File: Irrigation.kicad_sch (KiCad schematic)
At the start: 8 parts, among them J6 OSTVN02A150, J7 Conn_01x03, Q2 AS2302, Q4 PMH950UPEH

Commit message: 2nd rev schematic done
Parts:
- removed Q4: PMH950UPEH, SproutSenseFootprints:QPMOS1G2S3d_SOT8001_NEX, symbol SproutSense:PMH950UPEH
- removed R15: 4.7k, Resistor_SMD:R_0402_1005Metric, symbol Device:R_Small_US
- added Q3: SIUD412ED-T1-GE3, SMT_412ED-T1-GE3_VIS, symbol SproutSense:SIUD412ED-T1-GE3
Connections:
- net +5V: now also J7.2 (Pin_2); no longer R12.2
- net FLOW_SNS_ENA: now also R12.2, Q3.1 (G); no longer R12.1
- net GND: now also Q2.2 (S), R12.1, Q3.2 (S); no longer J7.3 (Pin_3)
- new net: J7.3 (Pin_3), Q3.3 (D)

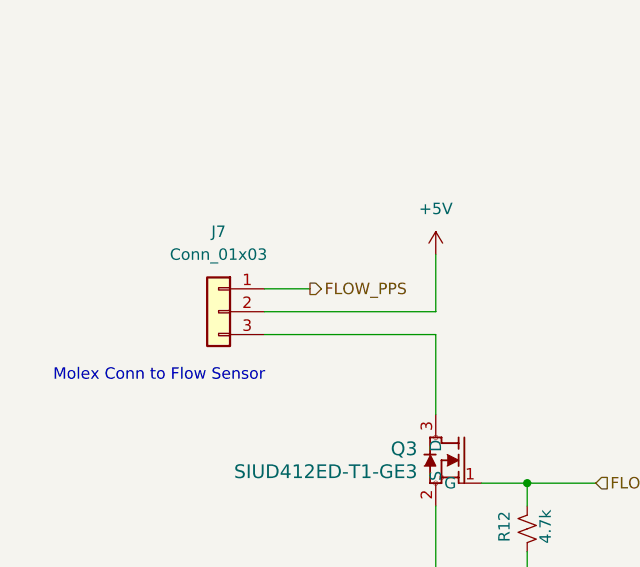
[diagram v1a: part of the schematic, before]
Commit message: mostly routed
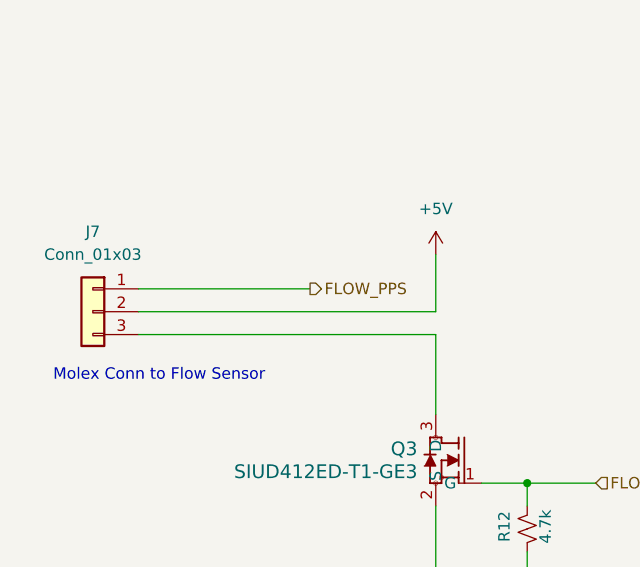
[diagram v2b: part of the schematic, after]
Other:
- moved on the sheet: J7
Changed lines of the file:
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@@
 	(wire
 		(pts
-			(xy 62.23 111.76) (xy 81.28 111.76)
+			(xy 48.26 111.76) (xy 81.28 111.76)
 		)
 		(stroke
@@
 	(wire
 		(pts
-			(xy 62.23 106.68) (xy 67.31 106.68)
+			(xy 48.26 106.68) (xy 67.31 106.68)
 		)
 		(stroke
@@
 	(wire
 		(pts
-			(xy 62.23 109.22) (xy 81.28 109.22)
+			(xy 48.26 109.22) (xy 81.28 109.22)
 		)
 		(stroke
@@
 			)
 		)
+		(property "MAXIMUM_PACKAGE_HEIGHT" ""
+			(at 156.21 105.41 90)
+			(effects
+				(font
+					(size 1.27 1.27)
+				)
+				(hide yes)
+			)
+		)
 		(pin "2"
 		)
@@
 			)
 		)
+		(property "MAXIMUM_PACKAGE_HEIGHT" ""
+			(at 182.88 77.47 0)
+			(effects
+				(font
+					(size 1.27 1.27)
+				)
+				(hide yes)
+			)
+		)
 		(pin "2"
 		)
@@
 			)
 		)
+		(property "MAXIMUM_PACKAGE_HEIGHT" ""
+			(at 99.06 128.27 0)
+			(effects
+				(font
+					(size 1.27 1.27)
+				)
+				(hide yes)
+			)
+		)
 		(pin "1"
 		)
@@
 			)
 		)
+		(property "MAXIMUM_PACKAGE_HEIGHT" ""
+			(at 162.56 78.74 90)
+			(effects
+				(font
+					(size 1.27 1.27)
+				)
+				(hide yes)
+			)
+		)
 		(pin "1"
 		)
@@
 	(symbol
 		(lib_id "Connector_Generic:Conn_01x03")
-		(at 57.15 109.22 0)
+		(at 43.18 109.22 0)
 		(mirror y)
 		(unit 1)
@@
 		(fields_autoplaced yes)
 		(property "Reference" "J7"
-			(at 57.15 100.33 0)
+			(at 43.18 100.33 0)
 			(effects
 				(font
@@
 		)
 		(property "Value" "Conn_01x03"
-			(at 57.15 102.87 0)
+			(at 43.18 102.87 0)
 			(effects
 				(font
@@
 		)
 		(property "Footprint" "Connector_PinHeader_1.00mm:PinHeader_1x03_P1.00mm_Vertical"
-			(at 57.15 109.22 0)
+			(at 43.18 109.22 0)
 			(effects
 				(font
@@
 		)
 		(property "Datasheet" "https://www.molex.com/content/dam/molex/molex-dot-com/products/automated/en-us/salesdrawingpdf/637/6373/022232031_sd.pdf?inline"
-			(at 57.15 109.22 0)
+			(at 43.18 109.22 0)
 			(effects
 				(font
@@
 		)
 		(property "Description" "CONN HEADER VERT 3POS 2.54MM"
-			(at 57.15 109.22 0)
+			(at 43.18 109.22 0)
 			(effects
 				(font
@@
 		)
 		(property "Distributor Prt #" "  WM4201-ND"
-			(at 57.15 109.22 0)
+			(at 43.18 109.22 0)
 			(effects
 				(font
@@
 		)
 		(property "Manuf Prt #" "0022232031"
-			(at 57.15 109.22 0)
+			(at 43.18 109.22 0)
+			(effects
+				(font
+					(size 1.27 1.27)
+				)
+				(hide yes)
+			)
+		)
+		(property "MAXIMUM_PACKAGE_HEIGHT" ""
+			(at 43.18 109.22 0)
 			(effects
 				(font
@@
 			)
 		)
+		(property "MAXIMUM_PACKAGE_HEIGHT" ""
+			(at 166.37 95.25 0)
+			(effects
+				(font
+					(size 1.27 1.27)
+				)
+				(hide yes)
+			)
+		)
 		(pin "1"
 		)
@@
 			(effects
 				(font
+					(size 1.27 1.27)
+				)
+				(hide yes)
+			)
+		)
+		(property "MAXIMUM_PACKAGE_HEIGHT" ""
+			(at 91.44 133.35 90)
+			(effects
+				(font

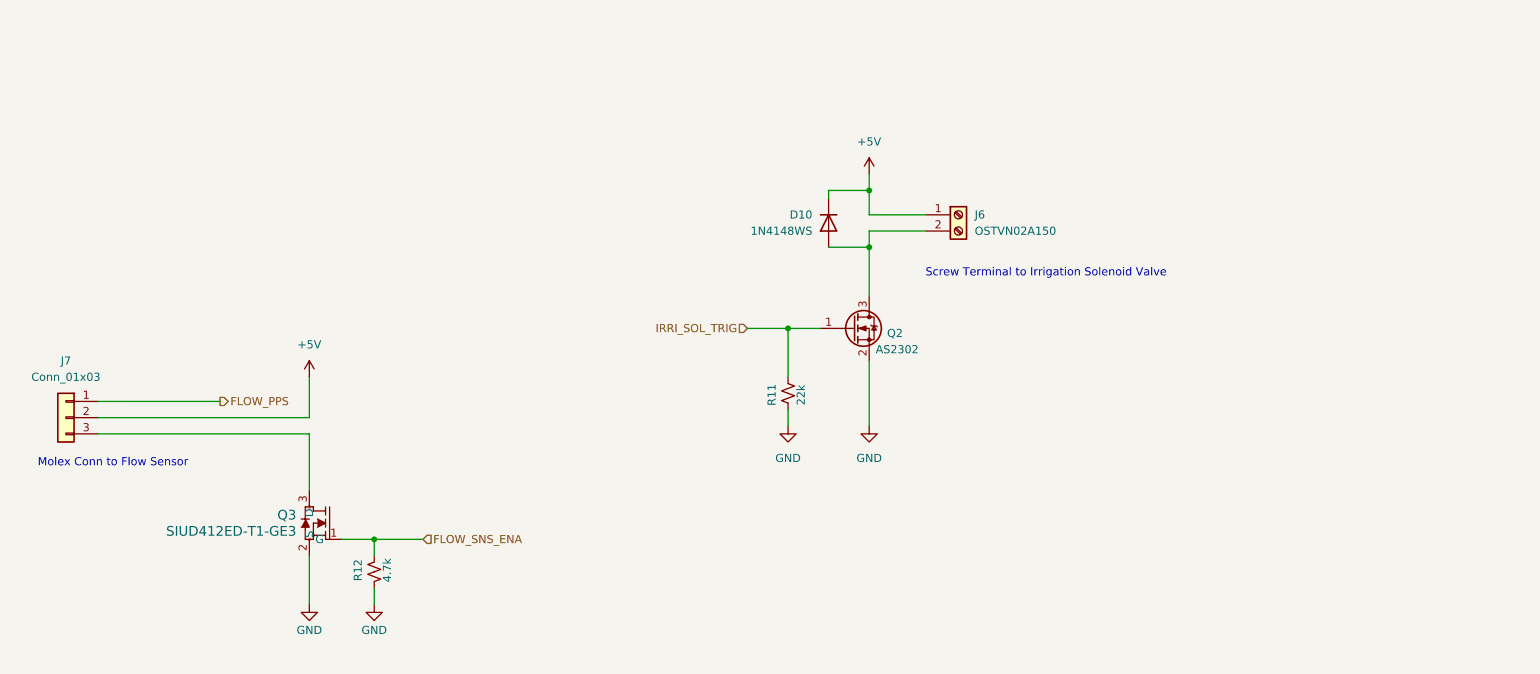
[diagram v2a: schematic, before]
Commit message: Removed via in pads
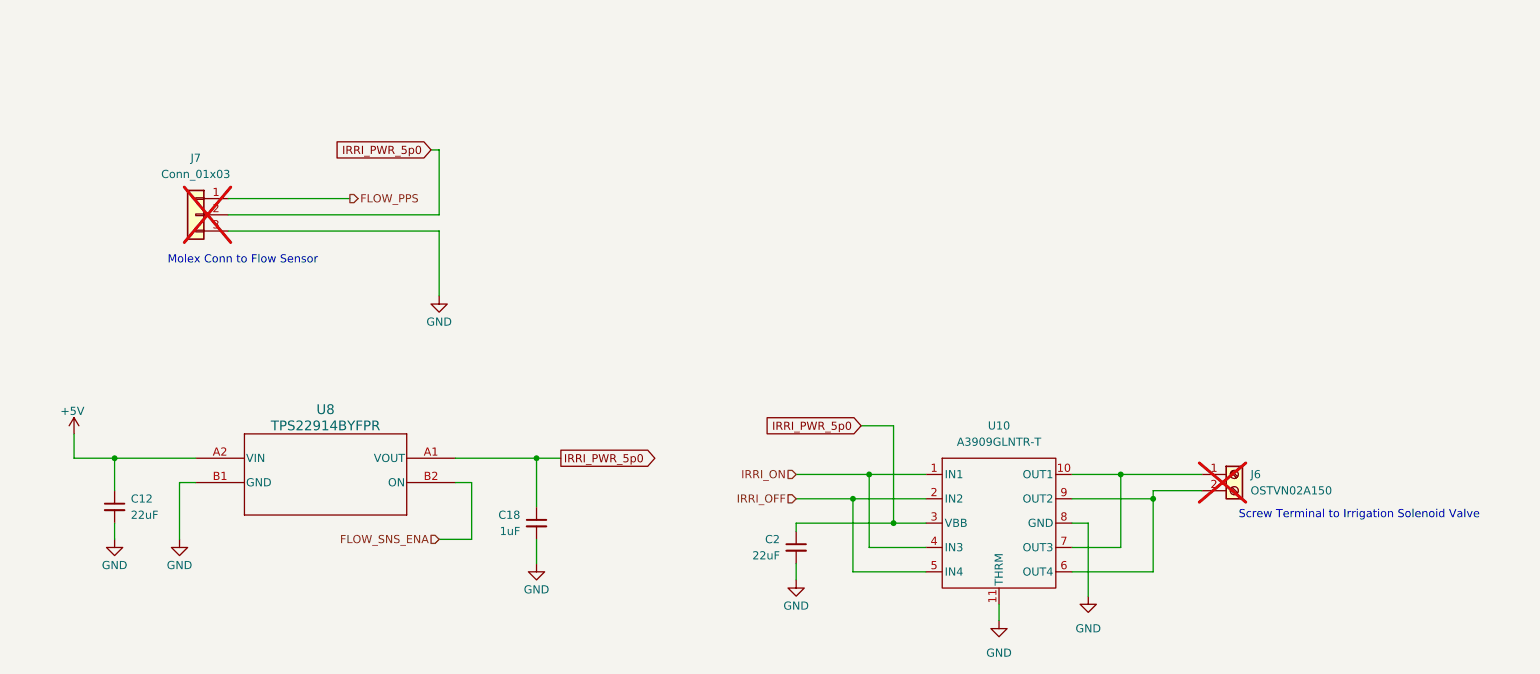
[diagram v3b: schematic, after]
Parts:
- removed D10: 1N4148WS, Diode_SMD:D_SOD-323, symbol Diode:1N4148WS
- removed Q2: AS2302, Package_TO_SOT_SMD:SOT-23, symbol Device:Q_NMOS_GSD
- removed Q3: SIUD412ED-T1-GE3, SMT_412ED-T1-GE3_VIS, symbol SproutSense:SIUD412ED-T1-GE3
- removed R11: 22k, Resistor_SMD:R_0402_1005Metric, symbol Device:R_Small_US
- removed R12: 4.7k, Resistor_SMD:R_0402_1005Metric, symbol Device:R_Small_US
- added C12, C2: 22uF, Capacitor_SMD:C_0402_1005Metric, symbol Device:C_Small
- added C18: 1uF, Capacitor_SMD:C_0402_1005Metric, symbol Device:C_Small
- added U10: A3909GLNTR-T, SproutSenseFootprints:SSOP-10-1EP_3.9x4.9mm_P1mm_EP2.1x3.3mm, symbol SproutSense:A3909
- added U8: TPS22914BYFPR, SproutSenseFootprints:YFP4_TEX, symbol SproutSense:TPS22914BYFPR
- J6, J7: now not fitted
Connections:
- net +5V: now also C12.1, U8.A2 (VIN); no longer J6.1 (Pin_1), J7.2 (Pin_2)
- net FLOW_SNS_ENA: now also U8.B2 (ON)
- net GND: now also J7.3 (Pin_3), C12.2, C18.2, C2.2, U10.11 (THRM), U10.8 (GND), U8.B1 (GND)
- net at J6.2 (Pin_2): now also U10.6 (OUT4), U10.9 (OUT2)
- new net: J6.1 (Pin_1), U10.10 (OUT1), U10.7 (OUT3)
- new net IRRI_OFF: U10.2 (IN2), U10.5 (IN4)
- new net IRRI_ON: U10.1 (IN1), U10.4 (IN3)
- new net IRRI_PWR_5p0: C18.1, C2.1, J7.2 (Pin_2), U10.3 (VBB), U8.A1 (VOUT)

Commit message: Swapped H bridge and irrigation conn
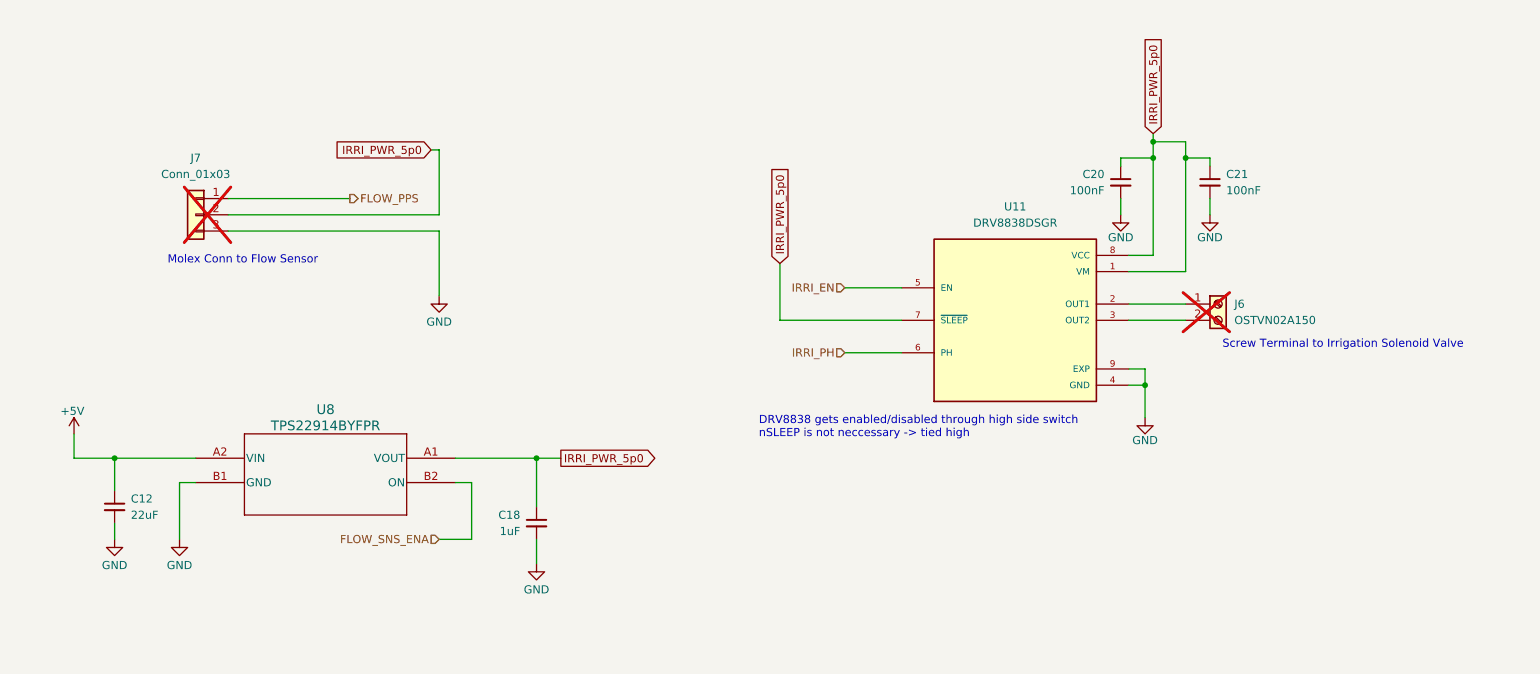
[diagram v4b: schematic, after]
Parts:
- removed C2: 22uF, Capacitor_SMD:C_0402_1005Metric, symbol Device:C_Small
- removed U10: A3909GLNTR-T, SproutSenseFootprints:SSOP-10-1EP_3.9x4.9mm_P1mm_EP2.1x3.3mm, symbol SproutSense:A3909
- added C20, C21: 100nF, Capacitor_SMD:C_0402_1005Metric, symbol Device:C_Small
- added U11: DRV8838DSGR, SproutSenseFootprints:SON50P200X200X80-9N, symbol SproutSense:DRV8838DSGR
- J7: footprint Connector_PinHeader_1.00mm:PinHeader_1x03_P1.00mm_Vertical -> SproutSenseFootprints:CONN_A-6373-03A_MOL
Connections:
- net GND: now also C20.2, C21.2, U11.4 (GND), U11.9 (EXP)
- net IRRI_PWR_5p0: now also C20.1, C21.1, U11.1 (VM), U11.7 (~{SLEEP}), U11.8 (VCC)
- net at J6.1 (Pin_1): now also U11.2 (OUT1)
- net at J6.2 (Pin_2): now also U11.3 (OUT2)
- new net IRRI_EN: U11.5 (EN)
- new net IRRI_PH: U11.6 (PH)
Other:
- note added: "DRV8838 gets enabled/disabled through high side switch nSLEEP is not neccessary -> tied high"
- moved on the sheet: J6
